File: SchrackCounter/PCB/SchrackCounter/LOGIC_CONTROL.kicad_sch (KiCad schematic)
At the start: 7 parts, among them U1 LTD080BUE-103A, U2 DC56-11EWA, U4 DC56-11EWA, U6 MAX7219

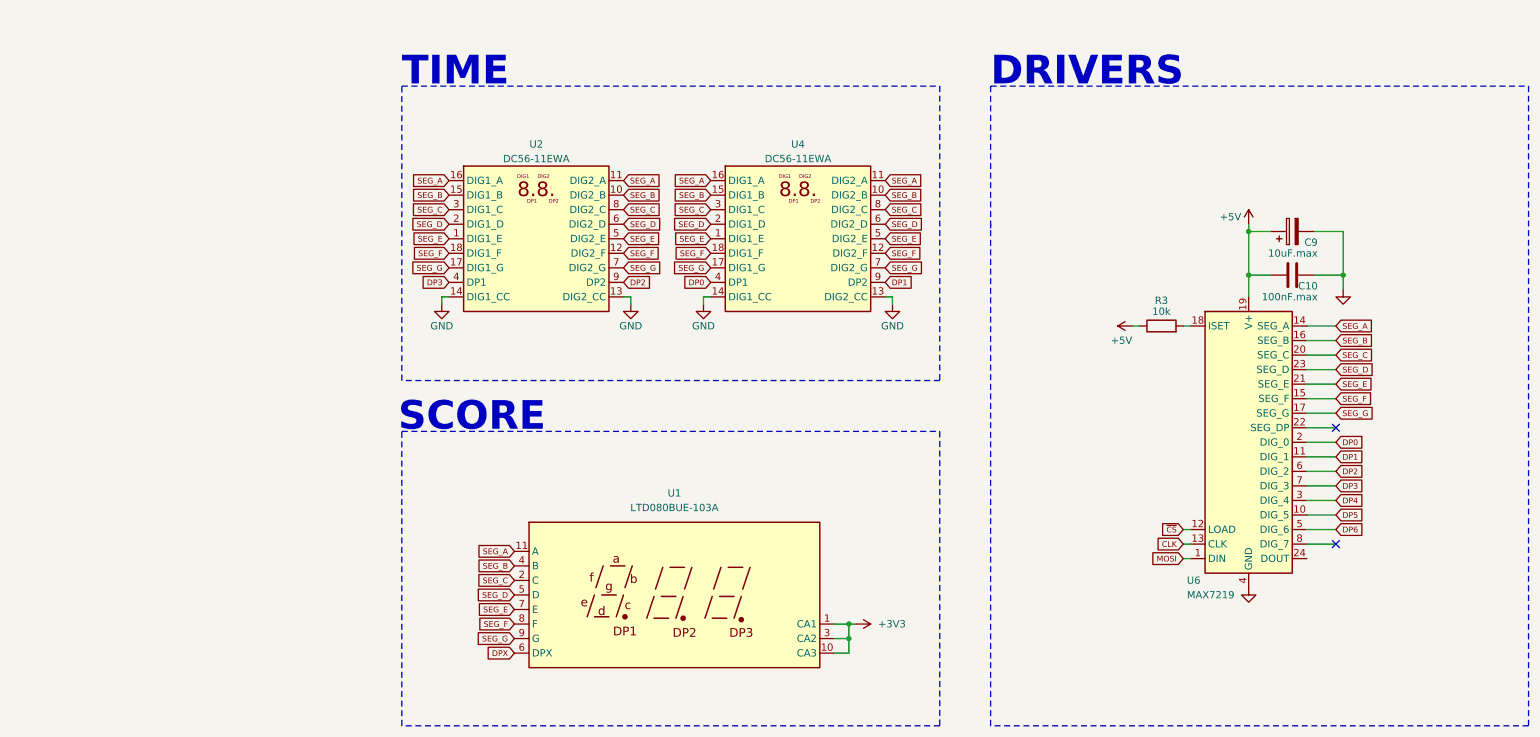
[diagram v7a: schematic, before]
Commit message: new custom symbol + footprint, pcb layout
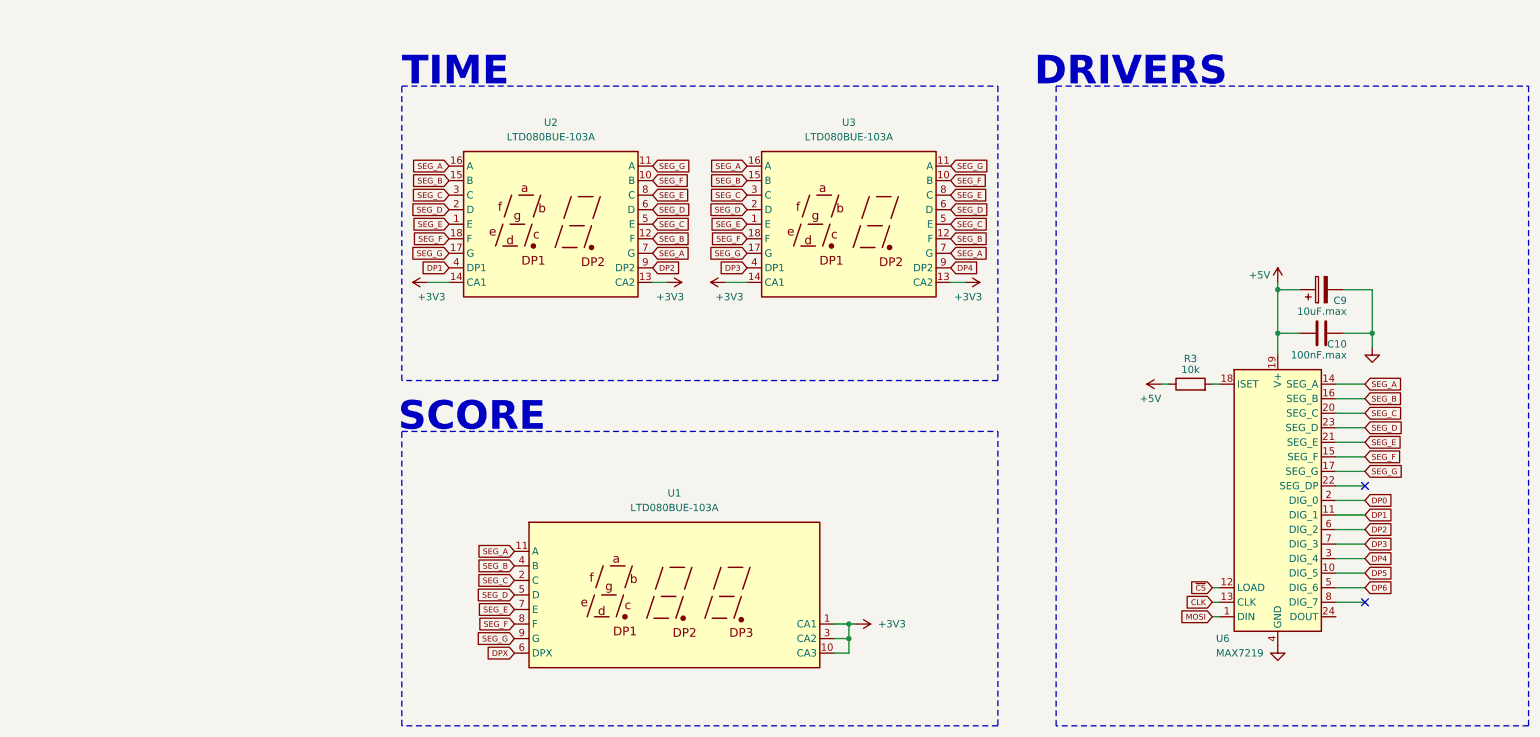
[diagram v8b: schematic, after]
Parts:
- removed U2, U4: DC56-11EWA, Display_7Segment:DA56-11SURKWA, symbol Display_Character:DC56-11EWA
- added U2, U3: LTD080BUE-103A, Schrack_brd:LDD080BUE-101A_made_by_bismarx, symbol sumec_sch_lib:LTD080BUE-103A_made_by_bismarx
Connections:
- net +3V3: now also U2.13 (CA2), U2.14 (CA1), U3.13 (CA2), U3.14 (CA1)
- net DP1: now also U2.4 (DP1)
- net DP2: now also U2.9 (DP2)
- net DP3: now also U3.4 (DP1)
- net DP4: now also U3.9 (DP2)
- net SEG_A: now also U2.16 (A), U2.7 (G), U3.16 (A), U3.7 (G)
- net SEG_B: now also U2.12 (F), U2.15 (B), U3.12 (F), U3.15 (B)
- net SEG_C: now also U2.3 (C), U2.5 (E), U3.3 (C), U3.5 (E)
- net SEG_D: now also U2.2 (D), U2.6 (D), U3.2 (D), U3.6 (D)
- net SEG_E: now also U2.1 (E), U2.8 (C), U3.1 (E), U3.8 (C)
- net SEG_F: now also U2.10 (B), U2.18 (F), U3.10 (B), U3.18 (F)
- net SEG_G: now also U2.11 (A), U2.17 (G), U3.11 (A), U3.17 (G)
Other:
- moved on the sheet: C10, C9, R3, U6
